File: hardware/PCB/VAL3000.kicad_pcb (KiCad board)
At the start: 4 copper layers, 40 x 50 mm, 60 parts, among them J1 1984617, J3 B4B-XH-A, J4 B4B-XH-A, J5 OSTVN02A150, J6 OSTVN02A150, J7 Conn_01x02_Pin, SW7 TS-1088-AR02016, SW8 TS-1088-AR02016, U1 RT9080-33GJ5, U2 TMC2209-LA-T, U3 TC-6615-4.5-160G, U4 TC-6615-4.5-160G, U5 TC-6615-4.5-160G, U6 ESP32-C3-WROOM-02, U9 AP63203QWU-7

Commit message: PCB
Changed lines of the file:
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@@
 			(drillshape 0)
 			(scaleselection 1)
-			(outputdirectory "G:/My Drive/Products/MorningRope/Hardware/PCB/10-27-25/")
+			(outputdirectory "G:/My Drive/Products/VAL-3000/PCB/11-28-25/")
 		)
 	)
@@
 		(at 0.43 -5.89)
 		(property "Reference" "SW7"
-			(at 2.14 2.08 180)
+			(at 3.07 -1.31 180)
 			(layer "F.SilkS")
 			(effects
@@
 		(tags "capacitor")
 		(property "Reference" "C51"
-			(at 2.15 0 0)
+			(at 2 -0.1 90)
 			(layer "F.SilkS")
 			(effects
@@
 		(tags "Through hole pin header THT 1x02 2.54mm single row")
 		(property "Reference" "J7"
-			(at 0.6 5.1 0)
+			(at -1.38 -2.014646 0)
 			(layer "F.SilkS")
 			(effects
 				(font
-					(size 1 1)
-					(thickness 0.15)
+					(size 0.6 0.6)
+					(thickness 0.1)
+					(bold yes)
 				)
 			)
@@
 		(at 0.43 -9.29)
 		(property "Reference" "SW8"
-			(at -3.25 -1.2 0)
+			(at 3.07 -1.21 0)
 			(layer "F.SilkS")
 			(effects
@@
 		(tags "OSTVN02A150 ")
 		(property "Reference" "J5"
-			(at 5.5 3.066 270)
+			(at 5.04 2.6 0)
 			(unlocked yes)
 			(layer "F.SilkS")
 			(effects
 				(font
-					(size 1 1)
-					(thickness 0.15)
+					(size 0.6 0.6)
+					(thickness 0.1)
+					(bold yes)
 				)
 			)
@@
 		(at -6.5 -5.45 180)
 		(property "Reference" "L2"
-			(at -2.55 0 90)
+			(at -2.5 -0.95 90)
 			(layer "F.SilkS")
 			(effects
@@
 		(tags "OSTVN02A150 ")
 		(property "Reference" "J6"
-			(at 5.5 3 90)
+			(at 5 2.7 0)
 			(unlocked yes)
 			(layer "F.SilkS")
 			(effects
 				(font
-					(size 1 1)
-					(thickness 0.15)
+					(size 0.6 0.6)
+					(thickness 0.1)
+					(bold yes)
 				)
 			)
@@
 		(tags "resistor")
 		(property "Reference" "R26"
-			(at -1.79 -0.1 90)
+			(at 1.88 -0.19 90)
 			(layer "F.SilkS")
 			(effects
@@
 		(tags "capacitor")
 		(property "Reference" "C25"
-			(at 1.83 0.05 90)
+			(at 0 -0.9 90)
 			(layer "F.SilkS")
 			(effects
@@
 	)
 	(gr_text "B"
-		(at 3.4 -9 0)
+		(at 3.4 -8.2 0)
 		(layer "F.SilkS")
 		(effects
@@
 	)
 	(gr_text "R"
-		(at 3.4 -5 0)
+		(at 3.4 -4.7 0)
 		(layer "F.SilkS")
 		(effects
@@
 	)
 	(segment
+		(start -4.1325 11.35)
+		(end -4.1325 13.7675)
+		(width 0.8)
+		(layer "F.Cu")
+		(net 2)
+	)
+	(segment
+		(start -4.1325 13.7675)
+		(end 2.5 20.4)
+		(width 0.8)
+		(layer "F.Cu")
+		(net 2)
+	)
+	(segment
 		(start -6.3 7.95)
 		(end -6.3 5.45)
@@
 	)
 	(segment
-		(start -4.1325 13.1675)
-		(end 3.1 20.4)
-		(width 0.8)
-		(layer "F.Cu")
-		(net 2)
-	)
-	(segment
 		(start -10.425 -2.875)
 		(end -10.9 -2.875)
@@
 	)
 	(segment
-		(start -10.7 -2.675)
-		(end -10.7 0.6)
+		(start 2.5 20.4)
+		(end 3.1 20.4)
 		(width 0.8)
 		(layer "F.Cu")
@@
 	)
 	(segment
-		(start -4.376 0.176)
-		(end -7.65 3.45)
+		(start -10.7 -2.675)
+		(end -10.7 0.6)
 		(width 0.8)
 		(layer "F.Cu")
@@
 	)
 	(segment
-		(start -4.1325 11.35)
-		(end -4.1325 13.1675)
+		(start -4.376 0.176)
+		(end -7.65 3.45)
 		(width 0.8)
 		(layer "F.Cu")

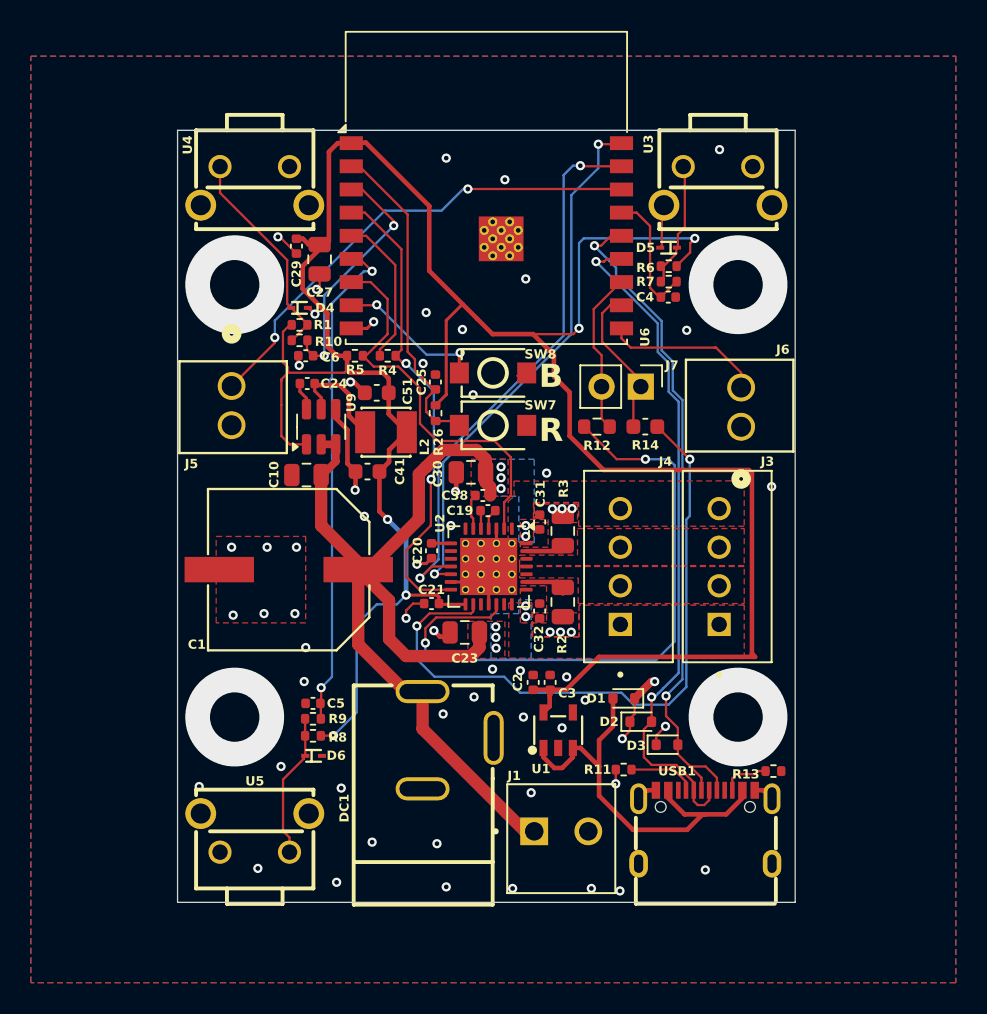
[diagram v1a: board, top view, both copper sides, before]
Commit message: Button fixes and PCB NEMA 17 holes
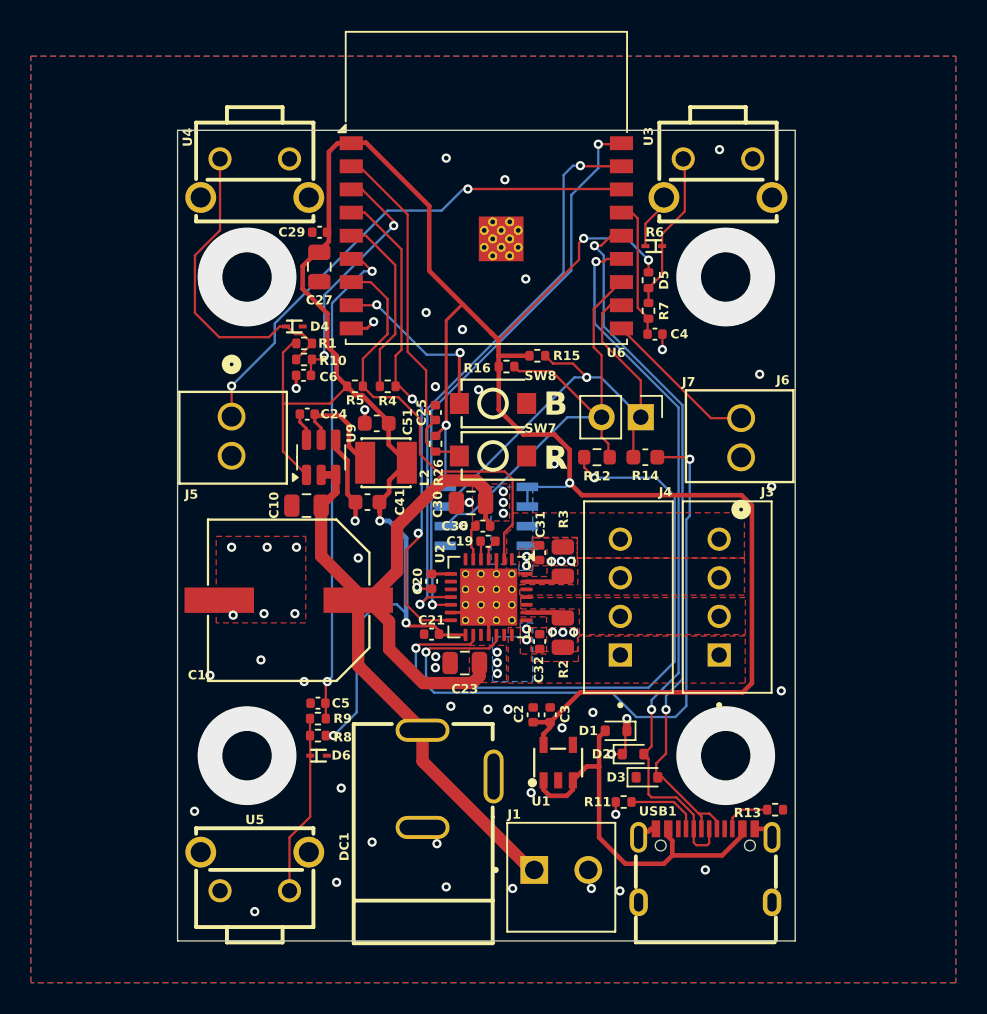
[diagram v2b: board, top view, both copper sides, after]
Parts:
- added R15: 5.1K, Resistor_SMD:R_0402_1005Metric, F.Cu at (3.30, -10.4)
- added R16: 5.1K, Resistor_SMD:R_0402_1005Metric, F.Cu at (1.30, -9.70)
- added U7: AS5600L-ASOM, AS5600L-ASOM_AMS:AS5600L-ASOM_AMS, B.Cu at (0.00, 0.00)
- moved C4 2.55 mm to (10.9, -11.8)
- moved R13 2.50 mm to (18.7, 19.0)
- moved DC1 2.50 mm to (-1.83, 17.0)
- moved J1 2.50 mm to (1.35, 26.9)
- moved U5 2.50 mm to (-15.0, 23.0)
- moved USB1 2.50 mm to (14.2, 22.6)
- moved D3 2.48 mm to (10.4, 16.9)
- moved R7 2.30 mm to (10.5, -13.3), turned to -90 degrees
- moved D1 2.16 mm to (8.40, 13.9)
- moved D2 2.16 mm to (9.50, 15.4)
- moved R11 2.10 mm to (8.89, 18.5)
- moved C2 2.10 mm to (3.03, 12.9)
- moved C3 2.10 mm to (4.13, 12.9)
- moved U1 2.10 mm to (4.65, 15.9)
- moved C23 1.98 mm to (-1.40, 9.50)
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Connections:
- net USER_1/STEP renamed USER_1/STEP/SCL
- net USER_2/DIR renamed USER_2/DIR/SDA
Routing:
- net USER_1/STEP/SCL: track 10.0 -> 32.5 mm, vias 0 -> 1
- net USER_2/DIR/SDA: track 10.6 -> 32.3 mm
- net GND: track 44.3 -> 32.7 mm, vias 67 -> 62
- net 3V3: track 164.0 -> 173.7 mm, vias 5 -> 7
- net Net-(D4-Pad1): track 14.0 -> 21.1 mm
- net USB_D-: track 44.1 -> 47.3 mm
- net TMC_EN: track 25.7 -> 28.1 mm
- net Net-(D6-Pad1): track 9.41 -> 11.7 mm
- net USER_4/END_2: track 31.4 -> 33.7 mm
- net INDEX: track 34.8 -> 37.1 mm
- net USB_D+: track 43.9 -> 46.2 mm
- net TMC_UART_TX: track 9.92 -> 11.9 mm
- net Net-(U6-IO9): track 9.78 -> 11.8 mm
- net Net-(U6-EN): track 21.3 -> 23.2 mm
- net Net-(D5-Pad1): track 8.06 -> 9.84 mm
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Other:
- board size 40 x 50 mm -> 40 x 52.5 mm
